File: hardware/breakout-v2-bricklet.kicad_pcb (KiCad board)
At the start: 2 copper layers, 20 x 25 mm, 7 parts, among them P1 CON-SENSOR2, P2 CONN_01X07, P3 CON-SENSOR2, U1 DRILL, U2 DRILL, U3 DRILL, U4 DRILL

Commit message: Add WEEE, CE and TF logos
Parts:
- added G***: LOGO, kicad-libraries:WEEE_7mm, B.Cu at (141.4, 91.3)
- added G***: Logo_31x31, kicad-libraries:Logo_31x31, F.Cu at (138.8, 98.5)
- added VAL: CE_5mm, kicad-libraries:CE_5mm, B.Cu at (130.0, 94.0)

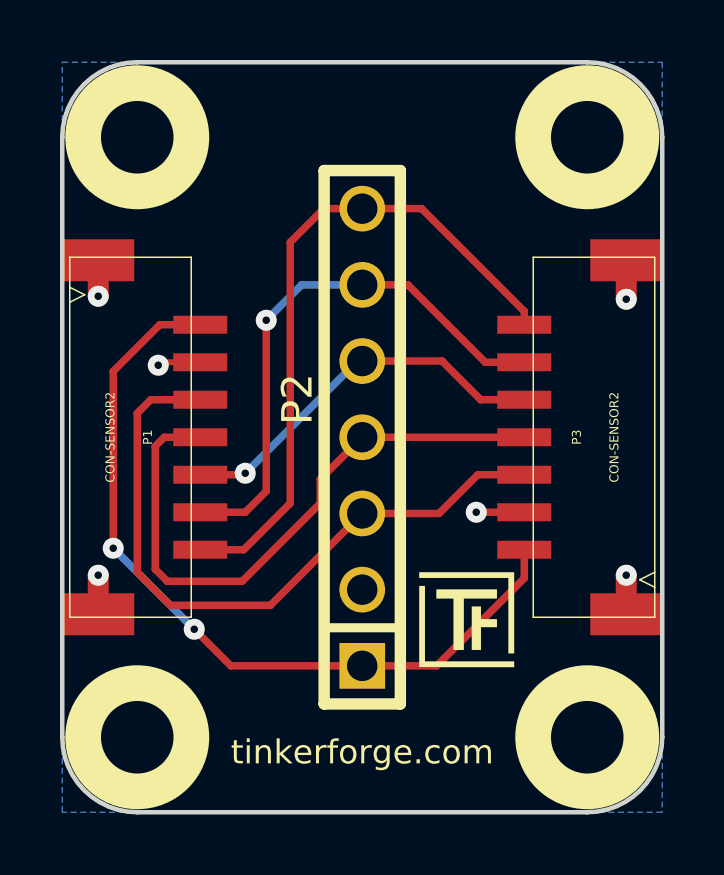
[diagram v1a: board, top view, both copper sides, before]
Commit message: Fix labeling and add fiducial marks
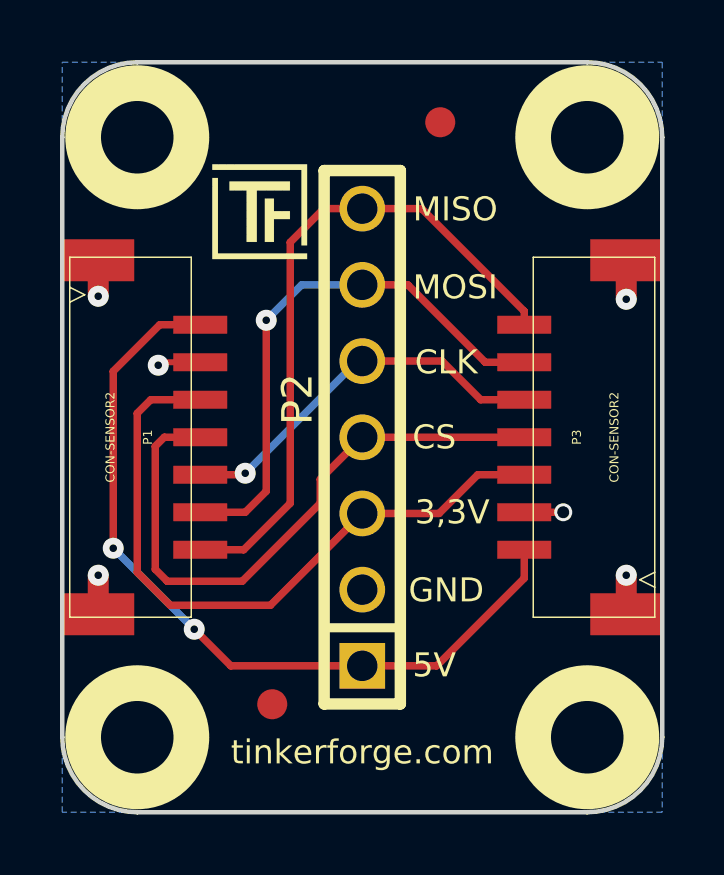
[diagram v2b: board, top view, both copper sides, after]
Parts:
- added Fiducial_Mark: VAL**, kicad-libraries:Fiducial_Mark, F.Cu at (133.9, 102.9)
- added Fiducial_Mark: VAL**, kicad-libraries:Fiducial_Mark, F.Cu at (139.5, 83.5)
- moved G*** 15.3 mm to (131.9, 84.9)
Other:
- board text added: "3,3V"
- board text added: "5V"
- board text added: "CLK"
- board text added: "CS"
- board text added: "GND"
- board text added: "MISO"
- board text added: "MOSI"
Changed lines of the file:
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@@
     (area 125.994999 80.594999 147.805001 107.405001)
     (thickness 1.6)
-    (drawings 9)
+    (drawings 16)
     (tracks 70)
     (zones 0)
-    (modules 10)
+    (modules 12)
     (nets 8)
   )
@@
   )
   (module kicad-libraries:Logo_31x31 (layer F.Cu)
-    (at 138.8 98.5)
+    (at 131.9 84.9)
     (fp_text reference G*** (at 1.34874 2.97434) (layer F.SilkS) hide
       (effects (font (size 0.29972 0.29972) (thickness 0.0762)))
@@
       (xy 3.1242 3.1242)) (layer F.SilkS) (width 0.00254))
   )
+  (module kicad-libraries:Fiducial_Mark (layer F.Cu)
+    (at 133.9 102.9)
+    (attr smd)
+    (fp_text reference Fiducial_Mark (at 0 0) (layer F.SilkS) hide
+      (effects (font (size 0.127 0.127) (thickness 0.03302)))
+    )
+    (fp_text value VAL** (at 0 -0.29972) (layer F.SilkS) hide
+      (effects (font (size 0.127 0.127) (thickness 0.03302)))
+    )
+    (fp_circle (center 0 0) (end 1.15062 0) (layer Dwgs.User) (width 0.01016))
+    (pad 1 smd circle (at 0 0) (size 1.00076 1.00076) (layers F.Cu F.Paste F.Mask)
+      (clearance 0.65024))
+  )
+  (module kicad-libraries:Fiducial_Mark (layer F.Cu)
+    (at 139.5 83.5)
+    (attr smd)
+    (fp_text reference Fiducial_Mark (at 0 0) (layer F.SilkS) hide
+      (effects (font (size 0.127 0.127) (thickness 0.03302)))
+    )
+    (fp_text value VAL** (at 0 -0.29972) (layer F.SilkS) hide
+      (effects (font (size 0.127 0.127) (thickness 0.03302)))
+    )
+    (fp_circle (center 0 0) (end 1.15062 0) (layer Dwgs.User) (width 0.01016))
+    (pad 1 smd circle (at 0 0) (size 1.00076 1.00076) (layers F.Cu F.Paste F.Mask)
+      (clearance 0.65024))
+  )
+  (gr_text MISO (at 140 86.4) (layer F.SilkS)
+    (effects (font (size 0.8 0.8) (thickness 0.15)))
+  )
+  (gr_text MOSI (at 140 89) (layer F.SilkS)
+    (effects (font (size 0.8 0.8) (thickness 0.15)))
+  )
+  (gr_text CLK (at 139.7 91.5) (layer F.SilkS)
+    (effects (font (size 0.8 0.8) (thickness 0.15)))
+  )
+  (gr_text CS (at 139.3 94) (layer F.SilkS)
+    (effects (font (size 0.8 0.8) (thickness 0.15)))
+  )
+  (gr_text 3,3V (at 139.9 96.5) (layer F.SilkS)
+    (effects (font (size 0.8 0.8) (thickness 0.15)))
+  )
+  (gr_text 5V (at 139.3 101.6) (layer F.SilkS)
+    (effects (font (size 0.8 0.8) (thickness 0.15)))
+  )
+  (gr_text GND (at 139.7 99.1) (layer F.SilkS)
+    (effects (font (size 0.8 0.8) (thickness 0.15)))
+  )
   (gr_line (start 146.9 104) (end 146.9 84) (angle 90) (layer Edge.Cuts) (width 0.15))
   (gr_line (start 129.4 106.5) (end 144.4 106.5) (angle 90) (layer Edge.Cuts) (width 0.15))
@@
   (segment (start 130.15 90.25) (end 128.6 91.8) (width 0.25) (layer F.Cu) (net 1))
   (segment (start 131.8 90.25) (end 131.25 90.25) (width 0.2) (layer F.Cu) (net 1))
-  (segment (start 142.3 96.5) (end 140.7 96.5) (width 0.25) (layer F.Cu) (net 2))
-  (via (at 140.7 96.5) (size 0.7) (drill 0.25) (layers F.Cu B.Cu) (net 2))
+  (segment (start 142.3 96.5) (end 143.6 96.5) (width 0.25) (layer F.Cu) (net 2))
+  (via (at 143.6 96.5) (size 0.6) (drill 0.4) (layers F.Cu B.Cu) (net 2))
   (segment (start 145.7 88.1) (end 145.7 89.4) (width 0.7) (layer F.Cu) (net 2))
   (via (at 145.7 89.4) (size 0.7) (drill 0.25) (layers F.Cu B.Cu) (net 2))

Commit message: Fix CE logo
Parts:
- moved VAL 0.30 mm to (130.0, 94.3), turned to 180 degrees
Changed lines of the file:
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@@
   (title_block
     (title "Breakout Bricklet V2")
-    (date 2017-02-28)
+    (date 2017-03-01)
     (rev 1.0)
     (company "Tinkerforge GmbH")
@@
   )
   (module kicad-libraries:CE_5mm (layer B.Cu)
-    (at 130 94)
-    (fp_text reference VAL (at 0 0) (layer B.SilkS) hide
+    (at 130 94.3 180)
+    (fp_text reference VAL (at 0 0 180) (layer B.SilkS) hide
       (effects (font (size 1.143 1.143) (thickness 0.1778)) (justify mirror))
     )
-    (fp_text value CE_5mm (at 0 0) (layer B.SilkS) hide
+    (fp_text value CE_5mm (at 0 0 180) (layer B.SilkS) hide
       (effects (font (size 1.143 1.143) (thickness 0.1778)) (justify mirror))
     )

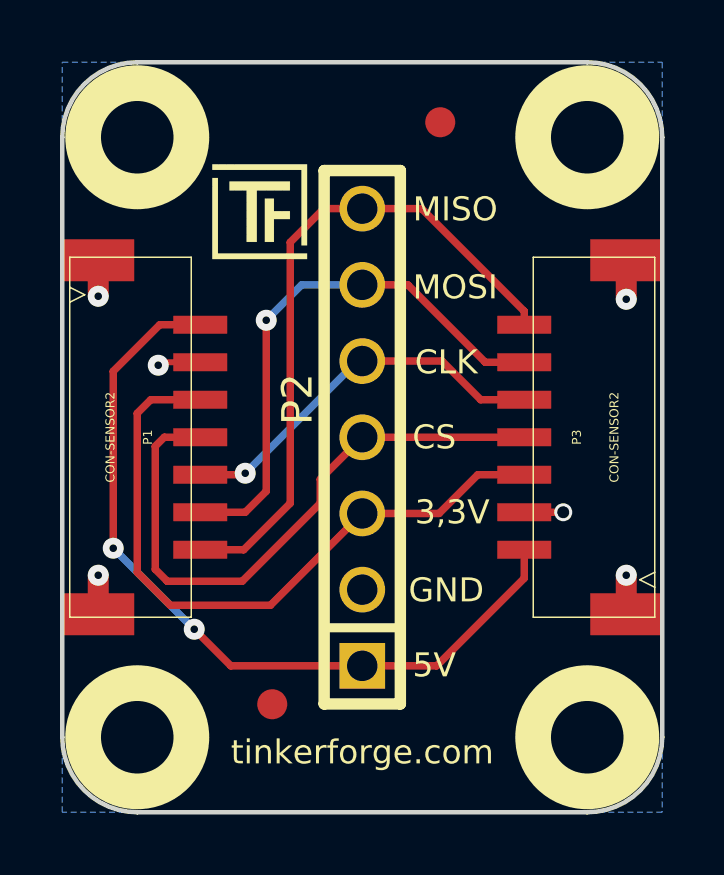
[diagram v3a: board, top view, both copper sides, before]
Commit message: Add 3d information
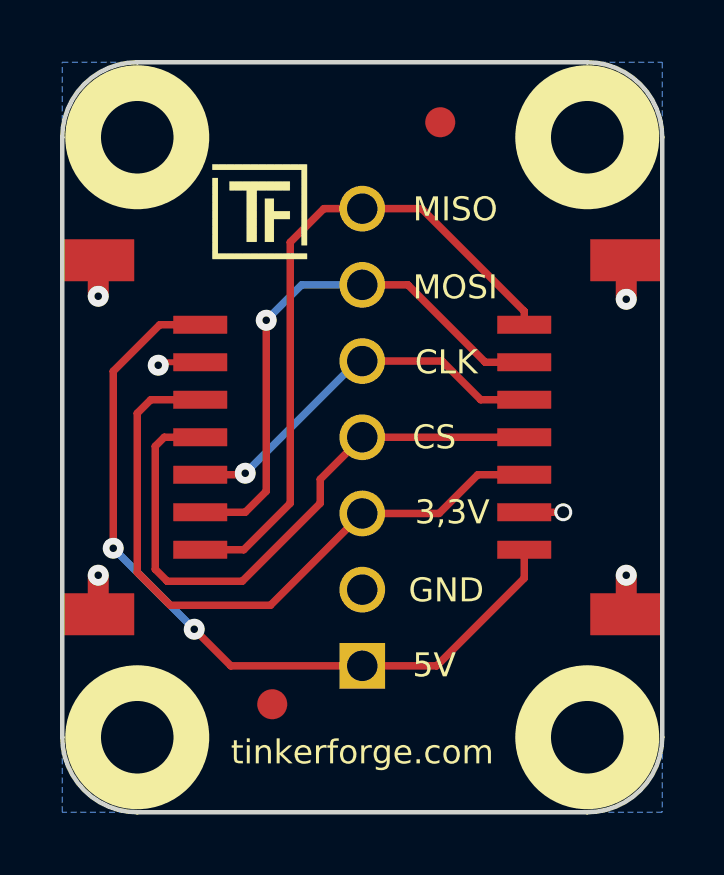
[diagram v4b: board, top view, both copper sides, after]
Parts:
- P1, P3: footprint CON-SENSOR2 -> kicad-libraries:CON-SENSOR2
- P2: footprint PIN_ARRAY-7X1 -> kicad-libraries:PIN_ARRAY-7X1
- U1, U2, U3, U4: footprint DRILL_NP -> kicad-libraries:DRILL_NP
